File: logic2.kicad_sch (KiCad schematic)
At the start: 45 parts, among them U12 IN74ALS02N (КР1533ЛЕ1), U14 SN74ALS86N (КР1533ЛП5), U15 CD4520АN (К561ИЕ10A), U21 SN74ALS14 (КР1533ТЛ2), U29 IN74ALS32N (КР1533ЛЛ1), U30 IN74ALS02N (КР1533ЛЕ1), U40 IN74ALS00N (КР1533ЛА3), U49 SN74ALS04 (КР1533ЛН1), U50 SN74ALS86N (КР1533ЛП5), U51 SN7486N (К155ЛП5)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

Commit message: Update for U21 fix (tape loading works now)
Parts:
- U21: value SN74ALS14 (КР1533ТЛ2) -> SN74ALS04 (КР1533ЛН1)
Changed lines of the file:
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@@
       (effects (font (size 1.27 1.27)))
     )
-    (property "Value" "SN74ALS14 (КР1533ТЛ2)" (at 837.565 234.315 0)
+    (property "Value" "SN74ALS04 (КР1533ЛН1)" (at 837.565 234.315 0)
       (effects (font (size 1.27 1.27)))
     )
@@
       (effects (font (size 1.27 1.27)))
     )
-    (property "Value" "SN74ALS14 (КР1533ТЛ2)" (at 85.09 154.305 0)
+    (property "Value" "SN74ALS04 (КР1533ЛН1)" (at 85.09 154.305 0)
       (effects (font (size 1.27 1.27)))
     )
@@
       (effects (font (size 1.27 1.27)))
     )
-    (property "Value" "SN74ALS14 (КР1533ТЛ2)" (at 149.225 153.67 0)
+    (property "Value" "SN74ALS04 (КР1533ЛН1)" (at 149.225 153.67 0)
       (effects (font (size 1.27 1.27)))
     )
@@
       (effects (font (size 1.27 1.27)))
     )
-    (property "Value" "SN74ALS14 (КР1533ТЛ2)" (at 117.475 153.67 0)
+    (property "Value" "SN74ALS04 (КР1533ЛН1)" (at 117.475 153.67 0)
       (effects (font (size 1.27 1.27)))
     )
@@
       (effects (font (size 1.27 1.27)))
     )
-    (property "Value" "SN74ALS14 (КР1533ТЛ2)" (at 789.94 234.315 0)
+    (property "Value" "SN74ALS04 (КР1533ЛН1)" (at 789.94 234.315 0)
       (effects (font (size 1.27 1.27)))
     )
@@
       (effects (font (size 1.27 1.27)))
     )
-    (property "Value" "SN74ALS14 (КР1533ТЛ2)" (at 814.07 234.315 0)
-      (effects (font (size 1.27 1.27)))
-    )
+    (property "Value" "SN74ALS04 (КР1533ЛН1)" (at 814.07 234.315 0)
+      (effects (font (size 1.27 1.27)))
+    )

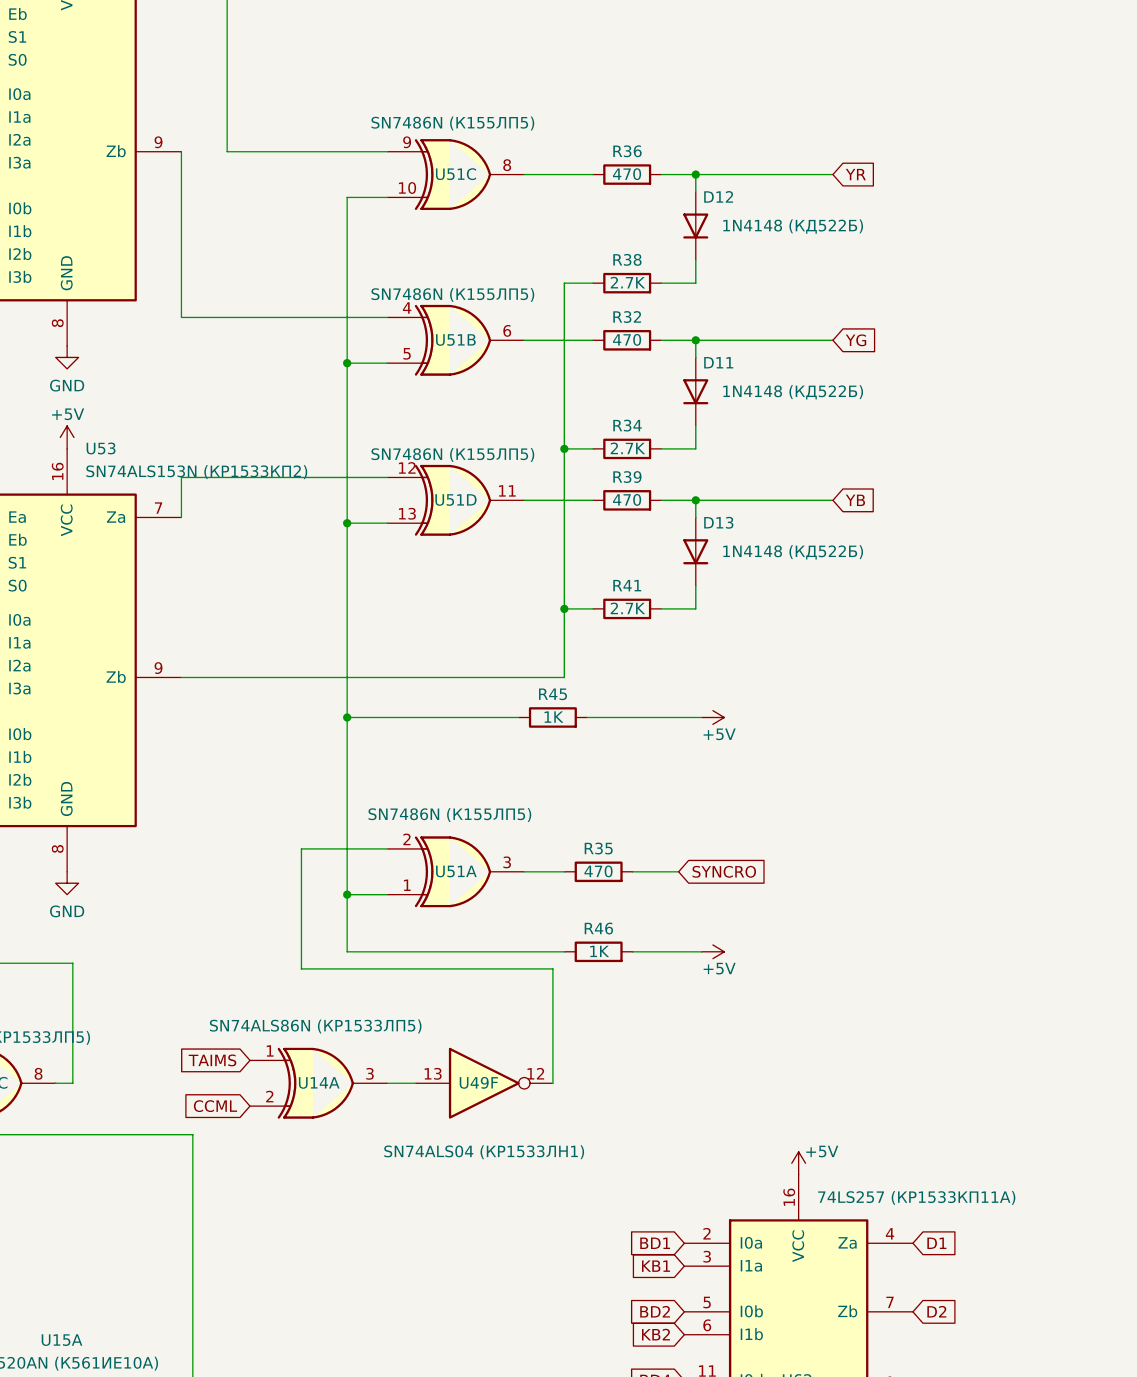
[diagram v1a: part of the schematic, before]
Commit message: Version 1.0 schematics and PCB complete
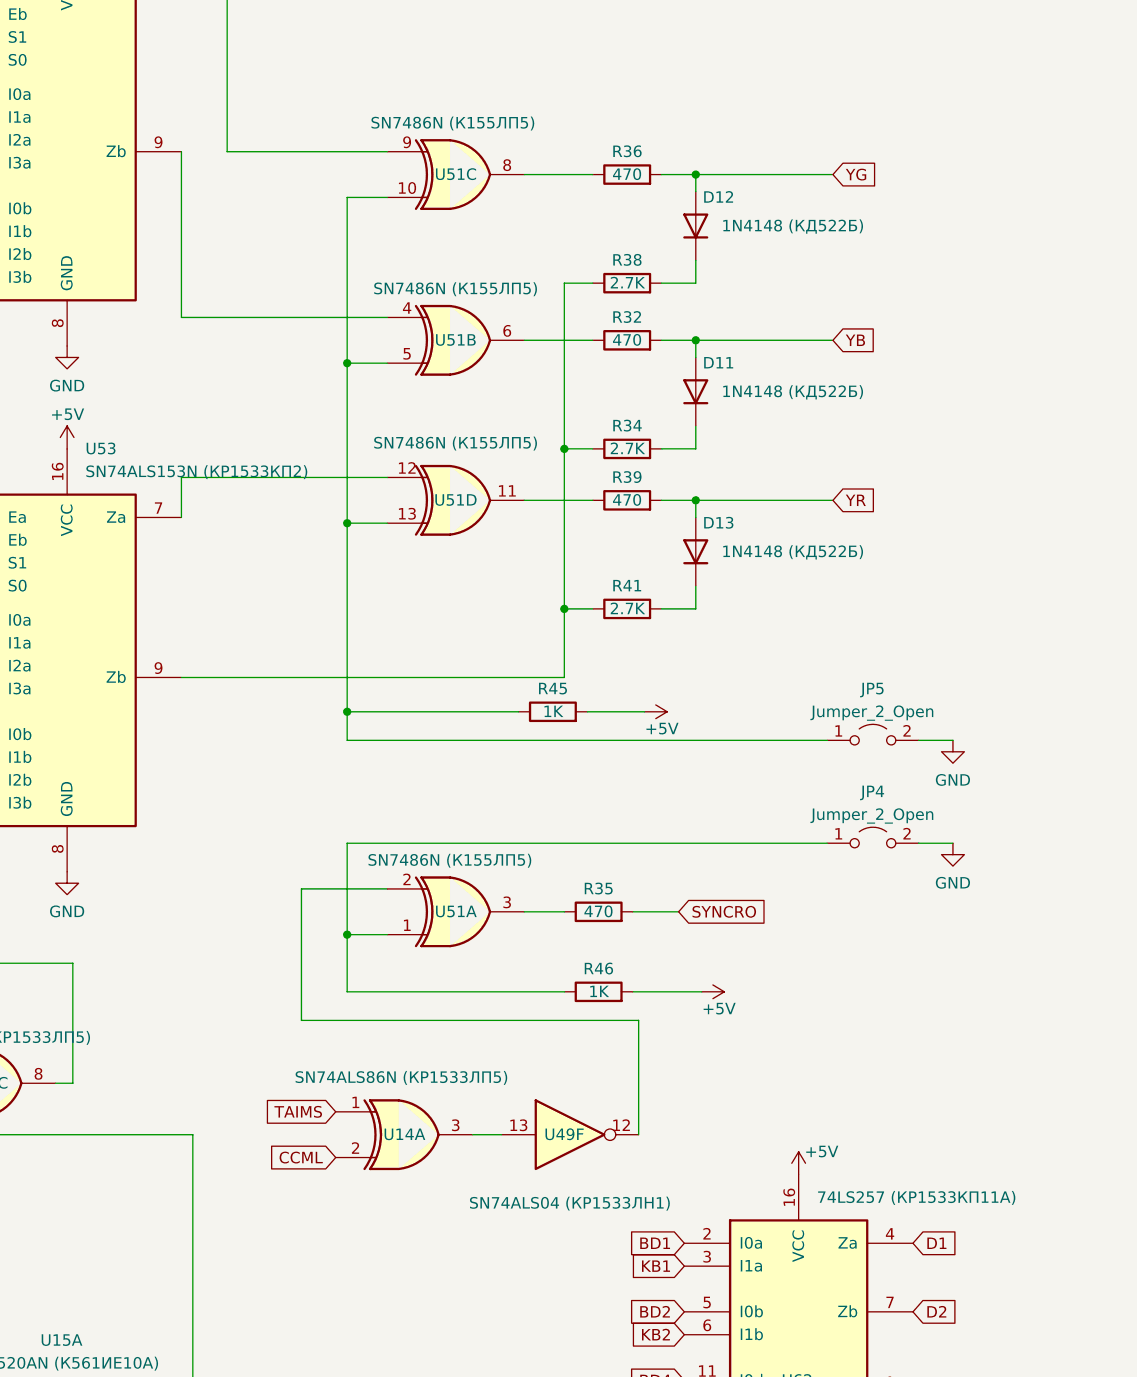
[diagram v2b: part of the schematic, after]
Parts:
- added JP4, JP5: Jumper_2_Open, Connector_PinHeader_2.54mm:PinHeader_1x02_P2.54mm_Vertical, symbol Delta_s_m_Lib:Jumper_2_Open
- C10, C11: symbol Device:C -> Delta_s_m_Lib:C
- C14: symbol Device:C_Polarized -> Delta_s_m_Lib:C_Polarized
- D11, D12, D13, D30, D31: symbol Device:D -> Delta_s_m_Lib:D
- R11, R12, R20, R21, R32, R34, R35, R36, R38, R39, R41, R45, R46: symbol Device:R -> Delta_s_m_Lib:R
- U12, U30: symbol 74xx:74LS02 -> Delta_s_m_Lib:74LS02
- U14, U50, U51: symbol 74xx:74LS86 -> Delta_s_m_Lib:74LS86
- U15: symbol w_connectors:CD4520АN_(К561ИЕ10) -> Delta_s_m_Lib:CD4520АN_(К561ИЕ10)
- U21: symbol 74xx:74LS14 -> Delta_s_m_Lib:74LS14
- U29: symbol 74xx:74LS32 -> Delta_s_m_Lib:74LS32
- U40: symbol 74xx:74LS00 -> Delta_s_m_Lib:74LS00
- U49: symbol 74xx:74LS04 -> Delta_s_m_Lib:74LS04
- U52: symbol w_connectors:SN74ALS175N -> Delta_s_m_Lib:SN74ALS175N
- U53, U60: symbol w_connectors:SN74ALS153N_(КР1533КП2) -> Delta_s_m_Lib:SN74ALS153N_(КР1533КП2)
- U54: symbol 74xx:74LS298 -> Delta_s_m_Lib:74LS298_2
- U55, U62: symbol 74xx:74LS257 -> Delta_s_m_Lib:74LS257_1
- U56: symbol w_connectors:SN74ALS175N_U56 -> Delta_s_m_Lib:SN74ALS175N_U56
- U57, U58, U64, U65: symbol w_connectors:SN74LS295N_(К555ИР16) -> Delta_s_m_Lib:SN74LS295N_(К555ИР16)
- U59: symbol w_connectors:SN74ALS175N -> Delta_s_m_Lib:SN74ALS175N_3
- U61: symbol 74xx:74LS298 -> Delta_s_m_Lib:74LS298_1
- U63: symbol w_connectors:SN74ALS175N_U63 -> Delta_s_m_Lib:SN74ALS175N_U63
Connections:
- net GND: now also JP4.2 (B), JP5.2 (B)
- net YB: now also D11.2 (A), R32.2; no longer D13.2 (A), R39.2
- net YG: now also D12.2 (A), R36.2; no longer D11.2 (A), R32.2
- net YR: now also D13.2 (A), R39.2; no longer D12.2 (A), R36.2
- net at R45.1, U51.10, U51.13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: now also JP5.1 (A); no longer R46.1, U51.1
- new net: JP4.1 (A), R46.1, U51.1
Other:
- moved on the sheet: R35, R45, R46, U14A, U49F, U51A

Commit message: Update
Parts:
- C14: footprint Capacitor_THT:CP_Radial_D10.0mm_P5.00mm -> Capacitor_THT:CP_Radial_D4.0mm_P2.00mm
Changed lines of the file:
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@@
       (effects (font (size 1.27 1.27)))
     )
-    (property "Footprint" "Capacitor_THT:CP_Radial_D10.0mm_P5.00mm" (at 62.865 148.9202 0)
+    (property "Footprint" "Capacitor_THT:CP_Radial_D4.0mm_P2.00mm" (at 62.865 148.9202 0)
       (effects (font (size 1.27 1.27)) hide)
     )

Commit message: Version 1.2 update
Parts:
- C10, C11: footprint Capacitor_THT:C_Disc_D7.0mm_W2.5mm_P5.00mm -> Delta_sm_lib:C_Disc_D7.0mm_W2.5mm_P5.00mm
- C14: value 4.7µF 15V -> 4.7µF 16V; footprint Capacitor_THT:CP_Radial_D4.0mm_P2.00mm -> Delta_sm_lib:CP_Radial_D4.0mm_P2.00mm
- D11, D12, D13, D30, D31: footprint Diode_THT:D_DO-35_SOD27_P10.16mm_Horizontal -> Delta_sm_lib:D_DO-35_SOD27_P10.16mm_Horizontal
- JP4, JP5: footprint Connector_PinHeader_2.54mm:PinHeader_1x02_P2.54mm_Vertical -> Delta_sm_lib:PinHeader_1x02_P2.54mm_Vertical
- R11, R12, R20, R21, R32, R34, R35, R36, R38, R39, R41, R45, R46: footprint Resistor_THT:R_Axial_DIN0207_L6.3mm_D2.5mm_P10.16mm_Horizontal -> Delta_sm_lib:R_Axial_DIN0207_L6.3mm_D2.5mm_P10.16mm_Horizontal
- U12, U14, U21, U29, U30, U40, U49, U50, U51, U57, U58, U64, U65: footprint Package_DIP:DIP-14_W7.62mm_Socket -> Delta_sm_lib:DIP-14_W7.62mm_Socket
- U15, U52, U53, U54, U55, U56, U59, U60, U61, U62, U63: footprint Package_DIP:DIP-16_W7.62mm_Socket -> Delta_sm_lib:DIP-16_W7.62mm_Socket

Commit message: Fixes
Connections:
- net YB: now also D12.2 (A), R36.2; no longer D11.2 (A), R32.2
- net YG: now also D13.2 (A), R39.2; no longer D12.2 (A), R36.2
- net YR: now also D11.2 (A), R32.2; no longer D13.2 (A), R39.2
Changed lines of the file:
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@@
     )
   )
-  (global_label "YB" (shape input) (at 370.205 71.12 0) (fields_autoplaced)
-    (effects (font (size 1.27 1.27)) (justify left))
-    (property "Intersheetrefs" "${INTERSHEET_REFS}" (at 375.4694 71.12 0)
+  (global_label "YR" (shape input) (at 370.205 71.12 0) (fields_autoplaced)
+    (effects (font (size 1.27 1.27)) (justify left))
+    (property "Intersheetrefs" "${INTERSHEET_REFS}" (at 375.5488 71.12 0)
       (effects (font (size 1.27 1.27)) (justify left) hide)
     )
@@
     )
   )
-  (global_label "YG" (shape input) (at 370.205 52.705 0) (fields_autoplaced)
-    (effects (font (size 1.27 1.27)) (justify left))
-    (property "Intersheetrefs" "${INTERSHEET_REFS}" (at 375.4694 52.705 0)
+  (global_label "YB" (shape input) (at 370.205 52.705 0) (fields_autoplaced)
+    (effects (font (size 1.27 1.27)) (justify left))
+    (property "Intersheetrefs" "${INTERSHEET_REFS}" (at 375.5488 52.705 0)
       (effects (font (size 1.27 1.27)) (justify left) hide)
     )
@@
     )
   )
-  (global_label "YR" (shape input) (at 370.205 88.9 0) (fields_autoplaced)
-    (effects (font (size 1.27 1.27)) (justify left))
-    (property "Intersheetrefs" "${INTERSHEET_REFS}" (at 375.4694 88.9 0)
-      (effects (font (size 1.27 1.27)) (justify left) hide)
-    )
+  (global_label "YG" (shape input) (at 370.205 88.9 0) (fields_autoplaced)
+    (effects (font (size 1.27 1.27)) (justify left))
+    (property "Intersheetrefs" "${INTERSHEET_REFS}" (at 375.5488 88.9 0)
+      (effects (font (size 1.27 1.27)) (justify left) hide)
+    )
